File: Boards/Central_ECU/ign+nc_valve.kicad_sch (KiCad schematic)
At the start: 23 parts, among them J1 Safety interlock, U3 TPS16630PWPR, U4 LM339, U5 TPS16630PWPR

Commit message: Some more minor tweaks
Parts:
- removed C29: 100n, Capacitor_SMD:C_0805_2012Metric, symbol Device:C
- removed C32: 22u, Capacitor_SMD:C_0805_2012Metric, symbol Device:C
- removed J1: Safety interlock, symbol Connector:Screw_Terminal_01x02
- removed R16: 4K5, Resistor_SMD:R_0805_2012Metric, symbol Device:R
- removed R17: 47K, Resistor_SMD:R_0805_2012Metric, symbol Device:R
- removed U5: TPS16630PWPR, Package_SO:HTSSOP-20-1EP_4.4x6.5mm_P0.65mm_EP3.4x6.5mm_Mask2.96x2.96mm_ThermalVias, symbol Power_Management:TPS16630PWPR
- added C29: 50u, symbol Device:C_Polarized
- added D2: D_Zener, symbol Device:D_Zener
- added F1: 2A, symbol Device:Fuse
- added Q3: DMT12H060LFDF-7, Package_DFN_QFN:Diodes_UDFN2020-6_Type-F, symbol Simulation_SPICE:NMOS
- added R29: 3.3K, Resistor_SMD:R_0805_2012Metric, symbol Device:R
- added R30: 549, Resistor_SMD:R_0805_2012Metric, symbol Device:R
- added R7: 121R, symbol Device:R
- added R9: 1K40, symbol Device:R
- added U5: LM1084-ADJ, symbol Regulator_Linear:LM1084-ADJ
- C28: value ? -> 10u; footprint Capacitor_SMD:C_0805_2012Metric -> (none); now fitted; now in the parts list
- C30: value 100n -> 22u
- C31: value 10u -> 22u
- R11: value 10K -> 0R; footprint Resistor_SMD:R_0805_2012Metric -> (none)
- R12: value 47K -> 35K7
- R15: value 10k -> 0R; footprint Resistor_SMD:R_0805_2012Metric -> (none)
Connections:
- net GND: now also U4.12 (V-), C29.2, D2.2 (A), Q3.3 (S), Q3.8 (S), R29.1, R9.2; no longer R15.2
- net at C17.1, C20.1, R8.1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: now also R15.1
- net OX_SOLENOID_-: now reaches U4.11 (+)
- net OX_SOLENOID_-: now also D2.1 (K), Q3.1 (D), Q3.2 (D), Q3.5 (D), Q3.6 (D), Q3.7 (D)
- net OX_SOLENOID_+: now reaches C31.1
- net OX_SOLENOID_+: now also C30.1, F1.2
- net 4S_ARMED_V+: now reaches C28.1
- net 4S_ARMED_V+: now also U5.3 (VI)
- net at U4.9 (+): now also R11.1, R15.2, C29.1, R7.1, U5.2 (VO)
- net VDDIO: now reaches U4.3 (V+)
- net VDDIO: now also R10.1
- removed net +3V3: R10.1, R11.1
- removed net ARM_VALVE: C30.1, R15.1
- net PGOOD_VALVE: no longer names the net of R11.2
- net PGOOD_VALVE: now also F1.1
- new net: Q3.4 (G), R30.2
- new net: R7.2, R9.1, U5.1 (ADJ)
- new net OX_FIRE: R29.2, R30.1
- no-connect marks 6 -> 3
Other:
- note added: "12V Regulator"
- note added: "Efficiency with 4s lipo input: Worst case 12/16.8 = 71% Typical case 12/14.8 = 81% Max power loss (16w servo) = 6.6W"
- note added: "IMON gives (IOUT*27.9u)*R volts With R=35700 is 0.996V/A At 4A will give 4V which is safe for 5V tollerant pins"
- note added: "Output requires some ESR for stablilty, namely zero at 50kHz. Datasheet reccomends 10u tantalum or 50u electrolytic. Could also look at ceramic with series resistor as per https://www.ti.com/document-viewer/lit/html/SSZTBJ1"
- note added: "Oxidider Solenoid Control"
- note added: "Vout = 1.25(1+R2/R1)"
- note removed: "IMON gives (IOUT*27.9u)*R volts With R=47000 is 1.311V/A"
- note removed: "NC Solenoid Valve"
- moved on the sheet: C17, C18, C19, C20, C21, R10, R12, R13, R14, R8, U3, U4A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

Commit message: Added most connectors and hooking up
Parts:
- removed D2: D_Zener, symbol Device:D_Zener
- removed R11, R15: 0R, symbol Device:R
- added D2: D_Schottky, symbol Device:D_Schottky
- added R16, R17, R18: 0R, symbol Device:R
- R14: value 4K5 -> 6K2
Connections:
- net 4S_ARMED_V+: now also R16.1, R17.2; no longer C28.1, U5.3 (VI)
- net OX_SOLENOID_+: now also D2.1 (K)
- net OX_SOLENOID_-: now also D2.2 (A)
- net Pyro Low Side/Ign+: now also F1.1
- net VDDIO: now also U4.10 (-), U4.4 (-), U4.6 (-), U4.8 (-)
- net at C17.1, C20.1, R8.1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: now also U4.9 (+), R17.1, R18.2
- net OX_LOW_SENSE: now reaches U4.13
- net at C29.1, R7.1, U5.2 (VO): now also R18.1; no longer U4.9 (+)
- net EMATCH_2_CONT: now reaches U4.1
- net 12V_SENSE: now reaches U4.14
- net EMATCH_1_CONT: now reaches U4.2
- net ARM_IGN renamed ARM_HS
- net IMON_IGN renamed IMON_HS
- net PGOOD_IGN renamed PGOOD_HS
- new net: C28.1, R16.2, U5.3 (VI)
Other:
- note added: "Bypass to allow for externally regulated power to be passed directly through. This will be useful if a 24V solenoid is used."
- note added: "High Side Switch"
- note added: "NFET good for 4.3A and V_DS of 115V. Max pulse 20A for 10us, ~1W continuous power dissapation."
- note added: "Ox Solenoid Control"
- note added: "Set to 3A max current"
- note removed: "Oxidider Solenoid Control"
- note removed: "Set to 4A max current"
- moved on the sheet: C17, C18, C19, C20, C21, C28, C29, C30, C31, F1, Q3, R10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

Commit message: For review
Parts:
- removed Q3: DMT12H060LFDF-7, Package_DFN_QFN:Diodes_UDFN2020-6_Type-F, symbol Simulation_SPICE:NMOS
- added Q1: DMT12H060LFDF, Package_DFN_QFN:Diodes_UDFN2020-6_Type-F, symbol TS_Symbols:DMT12H060LFDF
- added TP29: 12V, TestPoint:TestPoint_Keystone_5005-5009_Compact, symbol Connector:TestPoint_Small
- added TP30: ARMED, TestPoint:TestPoint_Keystone_5005-5009_Compact, symbol Connector:TestPoint_Small
- C21: renamed from C28; footprint (none) -> Capacitor_SMD:C_0805_2012Metric
- C22: renamed from C29; footprint (none) -> Capacitor_SMD:CP_Elec_6.3x9.9; MPN (none) -> 865080645012
- D5: renamed from D2; footprint (none) -> Diode_SMD:D_SOD-882; MPN (none) -> CTS05S40,L3F
- F1: footprint (none) -> Fuse:Fuse_1206_3216Metric
- R20: renamed from R17; footprint (none) -> Resistor_SMD:R_0805_2012Metric
- R21: renamed from R16; footprint (none) -> Resistor_SMD:R_0805_2012Metric
- R22: renamed from R18; footprint (none) -> Resistor_SMD:R_0805_2012Metric
- R23: renamed from R7; footprint (none) -> Resistor_SMD:R_0805_2012Metric
- R24: renamed from R9; footprint (none) -> Resistor_SMD:R_0805_2012Metric
- U4: value LM339 -> LM339B; footprint (none) -> Package_SO:TSSOP-14_4.4x5mm_P0.65mm; MPN (none) -> LM339BIPWR
- U5: footprint (none) -> Package_TO_SOT_SMD:TO-263-3_TabPin2; MPN (none) -> LM1084ISX-ADJ/NOPB
- U6: renamed from U3; MPN (none) -> TPS16630PWPR
- renumbered C30 to C23, C31 to C24, C17 to C25, C20 to C26, C21 to C27, C19 to C28, C18 to C29, R30 to R25, R29 to R26, R8 to R27, R10 to R28, R12 to R29, R13 to R30, R14 to R31
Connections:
- net GND: now also Q1.4, Q1.8 (S)
- net OX_SOLENOID_-: now also Q1.1, Q1.2 (D), Q1.5 (D), Q1.6 (D), Q1.7 (D)
- net Pyro Low Side/Ign+: now also TP30.1
- net at C25.1, C26.1, R20.1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: now also TP29.1
- net at R25.2: now also Q1.3
- no-connect marks 3 -> 4
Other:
- company: (none) -> Hybrid Test Stand 2025
- title: (none) -> Interlocked Components

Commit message: Changed to 0603 passives and added NRST line
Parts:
- C21, C23, C24, C25, C26, C27, C28, C29: footprint Capacitor_SMD:C_0805_2012Metric -> Capacitor_SMD:C_0603_1608Metric
- R20, R21, R22, R23, R24, R25, R26, R27, R28, R29, R30, R31: footprint Resistor_SMD:R_0805_2012Metric -> Resistor_SMD:R_0603_1608Metric
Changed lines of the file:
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@@
 			)
 		)
-		(property "Footprint" "Capacitor_SMD:C_0805_2012Metric"
+		(property "Footprint" "Capacitor_SMD:C_0603_1608Metric"
 			(at 63.1952 181.61 0)
 			(effects
@@
 			)
 		)
-		(property "Footprint" "Resistor_SMD:R_0805_2012Metric"
+		(property "Footprint" "Resistor_SMD:R_0603_1608Metric"
 			(at 83.058 212.09 90)
 			(effects
@@
 			)
 		)
-		(property "Footprint" "Resistor_SMD:R_0805_2012Metric"
+		(property "Footprint" "Resistor_SMD:R_0603_1608Metric"
 			(at 44.45 65.278 90)
 			(effects
@@
 			)
 		)
-		(property "Footprint" "Resistor_SMD:R_0805_2012Metric"
+		(property "Footprint" "Resistor_SMD:R_0603_1608Metric"
 			(at 290.068 104.14 90)
 			(effects
@@
 			)
 		)
-		(property "Footprint" "Capacitor_SMD:C_0805_2012Metric"
+		(property "Footprint" "Capacitor_SMD:C_0603_1608Metric"
 			(at 74.6252 181.61 0)
 			(effects
@@
 			)
 		)
-		(property "Footprint" "Resistor_SMD:R_0805_2012Metric"
+		(property "Footprint" "Resistor_SMD:R_0603_1608Metric"
 			(at 71.882 80.01 90)
 			(effects
@@
 			)
 		)
-		(property "Footprint" "Resistor_SMD:R_0805_2012Metric"
+		(property "Footprint" "Resistor_SMD:R_0603_1608Metric"
 			(at 33.782 57.15 90)
 			(effects
@@
 			)
 		)
-		(property "Footprint" "Resistor_SMD:R_0805_2012Metric"
+		(property "Footprint" "Resistor_SMD:R_0603_1608Metric"
 			(at 85.852 67.31 90)
 			(effects
@@
 			)
 		)
-		(property "Footprint" "Resistor_SMD:R_0805_2012Metric"
+		(property "Footprint" "Resistor_SMD:R_0603_1608Metric"
 			(at 144.272 215.9 90)
 			(effects
@@
 			)
 		)
-		(property "Footprint" "Capacitor_SMD:C_0805_2012Metric"
+		(property "Footprint" "Capacitor_SMD:C_0603_1608Metric"
 			(at 152.0952 181.61 0)
 			(effects
@@
 			)
 		)
-		(property "Footprint" "Resistor_SMD:R_0805_2012Metric"
+		(property "Footprint" "Resistor_SMD:R_0603_1608Metric"
 			(at 115.57 160.528 90)
 			(effects
@@
 			)
 		)
-		(property "Footprint" "Capacitor_SMD:C_0805_2012Metric"
+		(property "Footprint" "Capacitor_SMD:C_0603_1608Metric"
 			(at 48.5648 200.66 0)
 			(effects
@@
 			)
 		)
-		(property "Footprint" "Capacitor_SMD:C_0805_2012Metric"
+		(property "Footprint" "Capacitor_SMD:C_0603_1608Metric"
 			(at 275.2852 71.12 0)
 			(effects
@@
 			)
 		)
-		(property "Footprint" "Resistor_SMD:R_0805_2012Metric"
+		(property "Footprint" "Resistor_SMD:R_0603_1608Metric"
 			(at 125.73 65.278 90)
 			(effects
@@
 			)
 		)
-		(property "Footprint" "Capacitor_SMD:C_0805_2012Metric"
+		(property "Footprint" "Capacitor_SMD:C_0603_1608Metric"
 			(at 70.1548 215.9 0)
 			(effects
@@
 			)
 		)
-		(property "Footprint" "Resistor_SMD:R_0805_2012Metric"
+		(property "Footprint" "Resistor_SMD:R_0603_1608Metric"
 			(at 304.8 97.028 90)
 			(effects
@@
 			)
 		)
-		(property "Footprint" "Resistor_SMD:R_0805_2012Metric"
+		(property "Footprint" "Resistor_SMD:R_0603_1608Metric"
 			(at 155.702 208.28 90)
 			(effects
@@
 			)
 		)
-		(property "Footprint" "Capacitor_SMD:C_0805_2012Metric"
+		(property "Footprint" "Capacitor_SMD:C_0603_1608Metric"
 			(at 263.8552 71.12 0)
 			(effects
@@
 			)
 		)
-		(property "Footprint" "Resistor_SMD:R_0805_2012Metric"
+		(property "Footprint" "Resistor_SMD:R_0603_1608Metric"
 			(at 155.702 191.77 90)
 			(effects
@@
 			)
 		)
-		(property "Footprint" "Capacitor_SMD:C_0805_2012Metric"
+		(property "Footprint" "Capacitor_SMD:C_0603_1608Metric"
 			(at 54.3052 71.12 0)
 			(effects

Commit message: More progress on layout
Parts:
- C26, C27: footprint Capacitor_SMD:C_0603_1608Metric -> Capacitor_SMD:C_1206_3216Metric
- R20, R21, R22: footprint Resistor_SMD:R_0603_1608Metric -> Resistor_SMD:R_1206_3216Metric
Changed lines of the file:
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@@
 			)
 		)
-		(property "Footprint" "Resistor_SMD:R_0603_1608Metric"
+		(property "Footprint" "Resistor_SMD:R_1206_3216Metric"
 			(at 44.45 65.278 90)
 			(effects
@@
 			)
 		)
-		(property "Footprint" "Capacitor_SMD:C_0603_1608Metric"
+		(property "Footprint" "Capacitor_SMD:C_1206_3216Metric"
 			(at 74.6252 181.61 0)
 			(effects
@@
 			)
 		)
-		(property "Footprint" "Resistor_SMD:R_0603_1608Metric"
+		(property "Footprint" "Resistor_SMD:R_1206_3216Metric"
 			(at 33.782 57.15 90)
 			(effects
@@
 			)
 		)
-		(property "Footprint" "Capacitor_SMD:C_0603_1608Metric"
+		(property "Footprint" "Capacitor_SMD:C_1206_3216Metric"
 			(at 152.0952 181.61 0)
 			(effects
@@
 			)
 		)
-		(property "Footprint" "Resistor_SMD:R_0603_1608Metric"
+		(property "Footprint" "Resistor_SMD:R_1206_3216Metric"
 			(at 125.73 65.278 90)
 			(effects

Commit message: Finished central ECU for review
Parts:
- TP29, TP30: footprint TestPoint:TestPoint_Keystone_5005-5009_Compact -> TestPoint:TestPoint_Pad_1.5x1.5mm
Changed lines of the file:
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@@
 	(title_block
 		(title "Interlocked Components")
-		(date "2025-04-02")
+		(date "2025-04-13")
 		(rev "A")
 		(company "Hybrid Test Stand 2025")
@@
 			)
 		)
-		(property "Footprint" "TestPoint:TestPoint_Keystone_5005-5009_Compact"
+		(property "Footprint" "TestPoint:TestPoint_Pad_1.5x1.5mm"
 			(at 182.88 173.99 0)
 			(effects
@@
 			)
 		)
-		(property "Footprint" "TestPoint:TestPoint_Keystone_5005-5009_Compact"
+		(property "Footprint" "TestPoint:TestPoint_Pad_1.5x1.5mm"
 			(at 143.51 101.6 0)
 			(effects

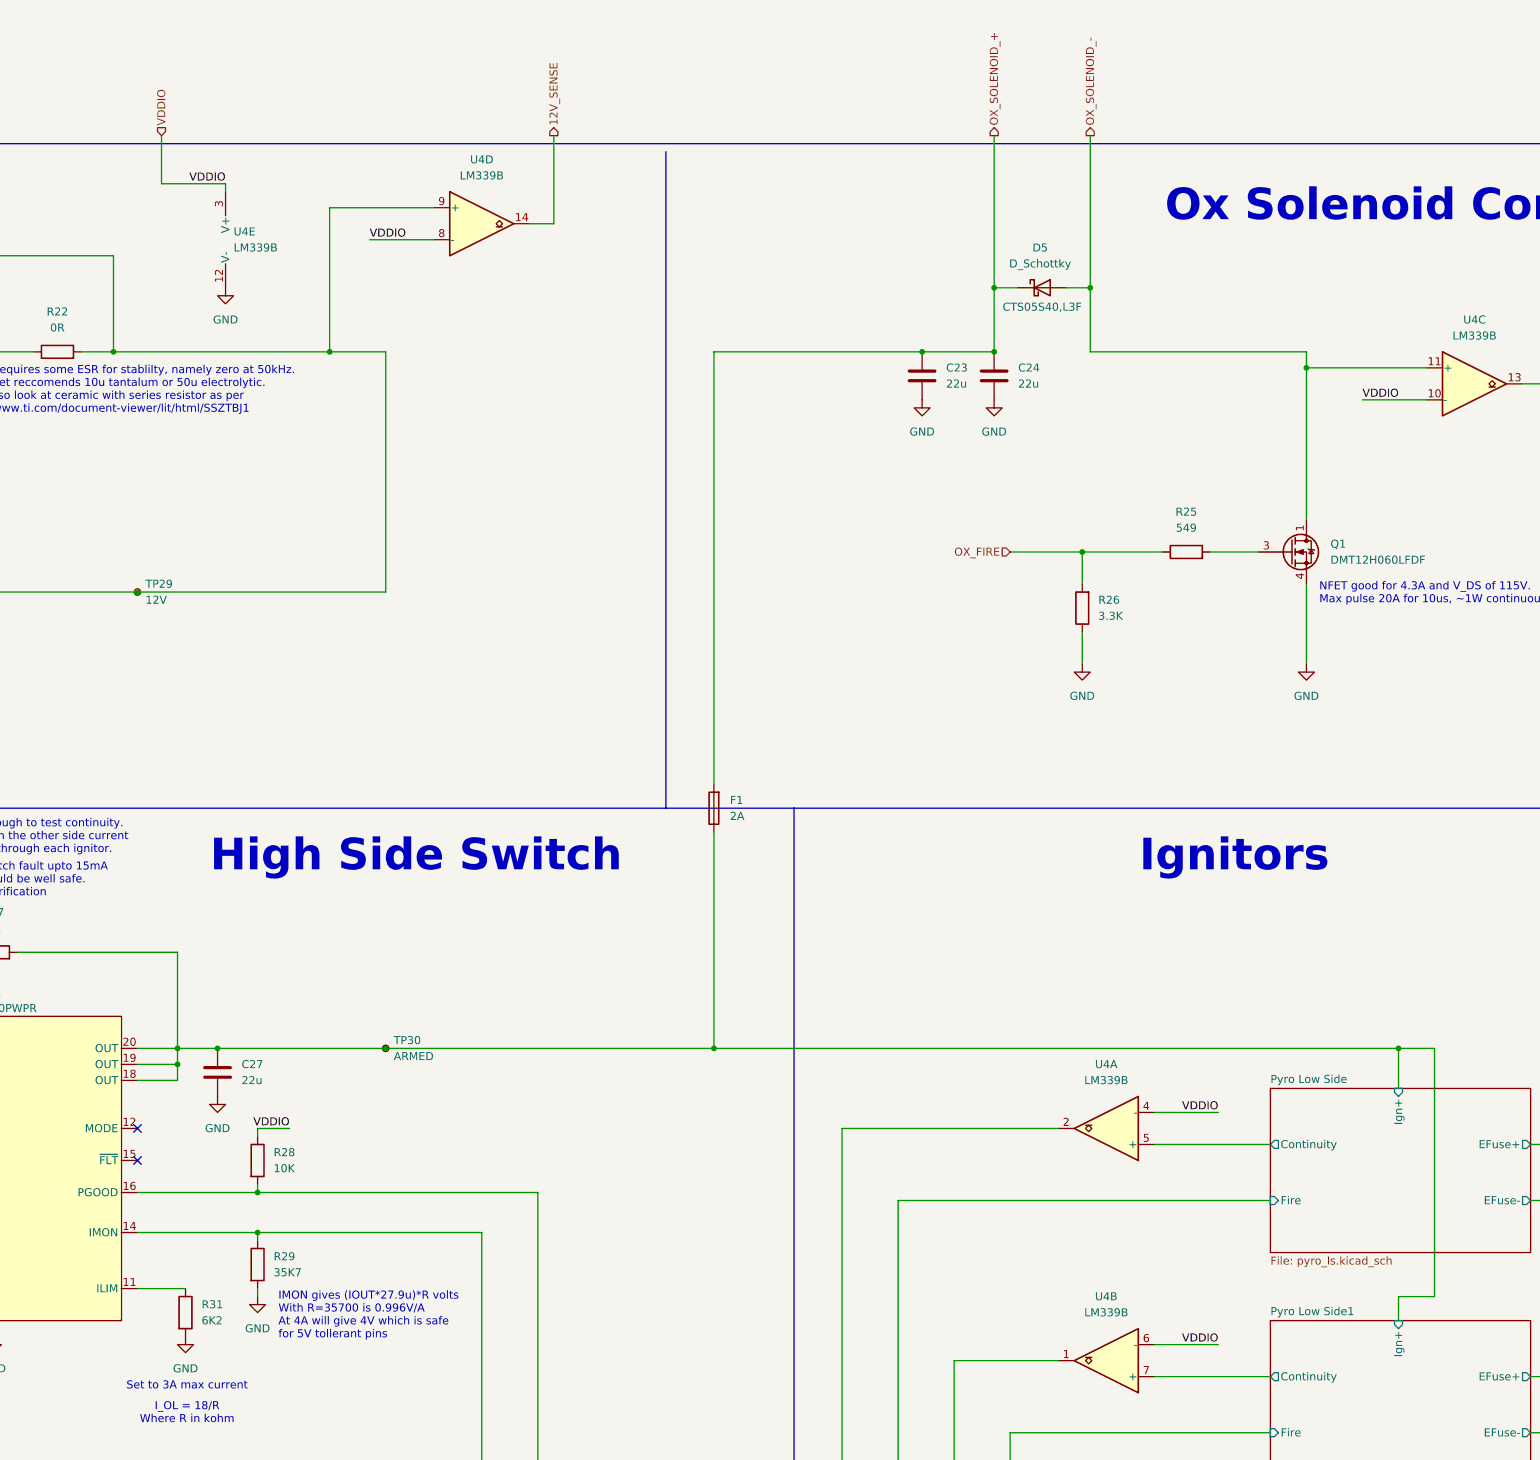
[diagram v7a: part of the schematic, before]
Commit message: Fixed voltage divider and comparator bias
Re feedback from Chris still need to fix regulator power dissipation. Happy with other points being non-issues at current.
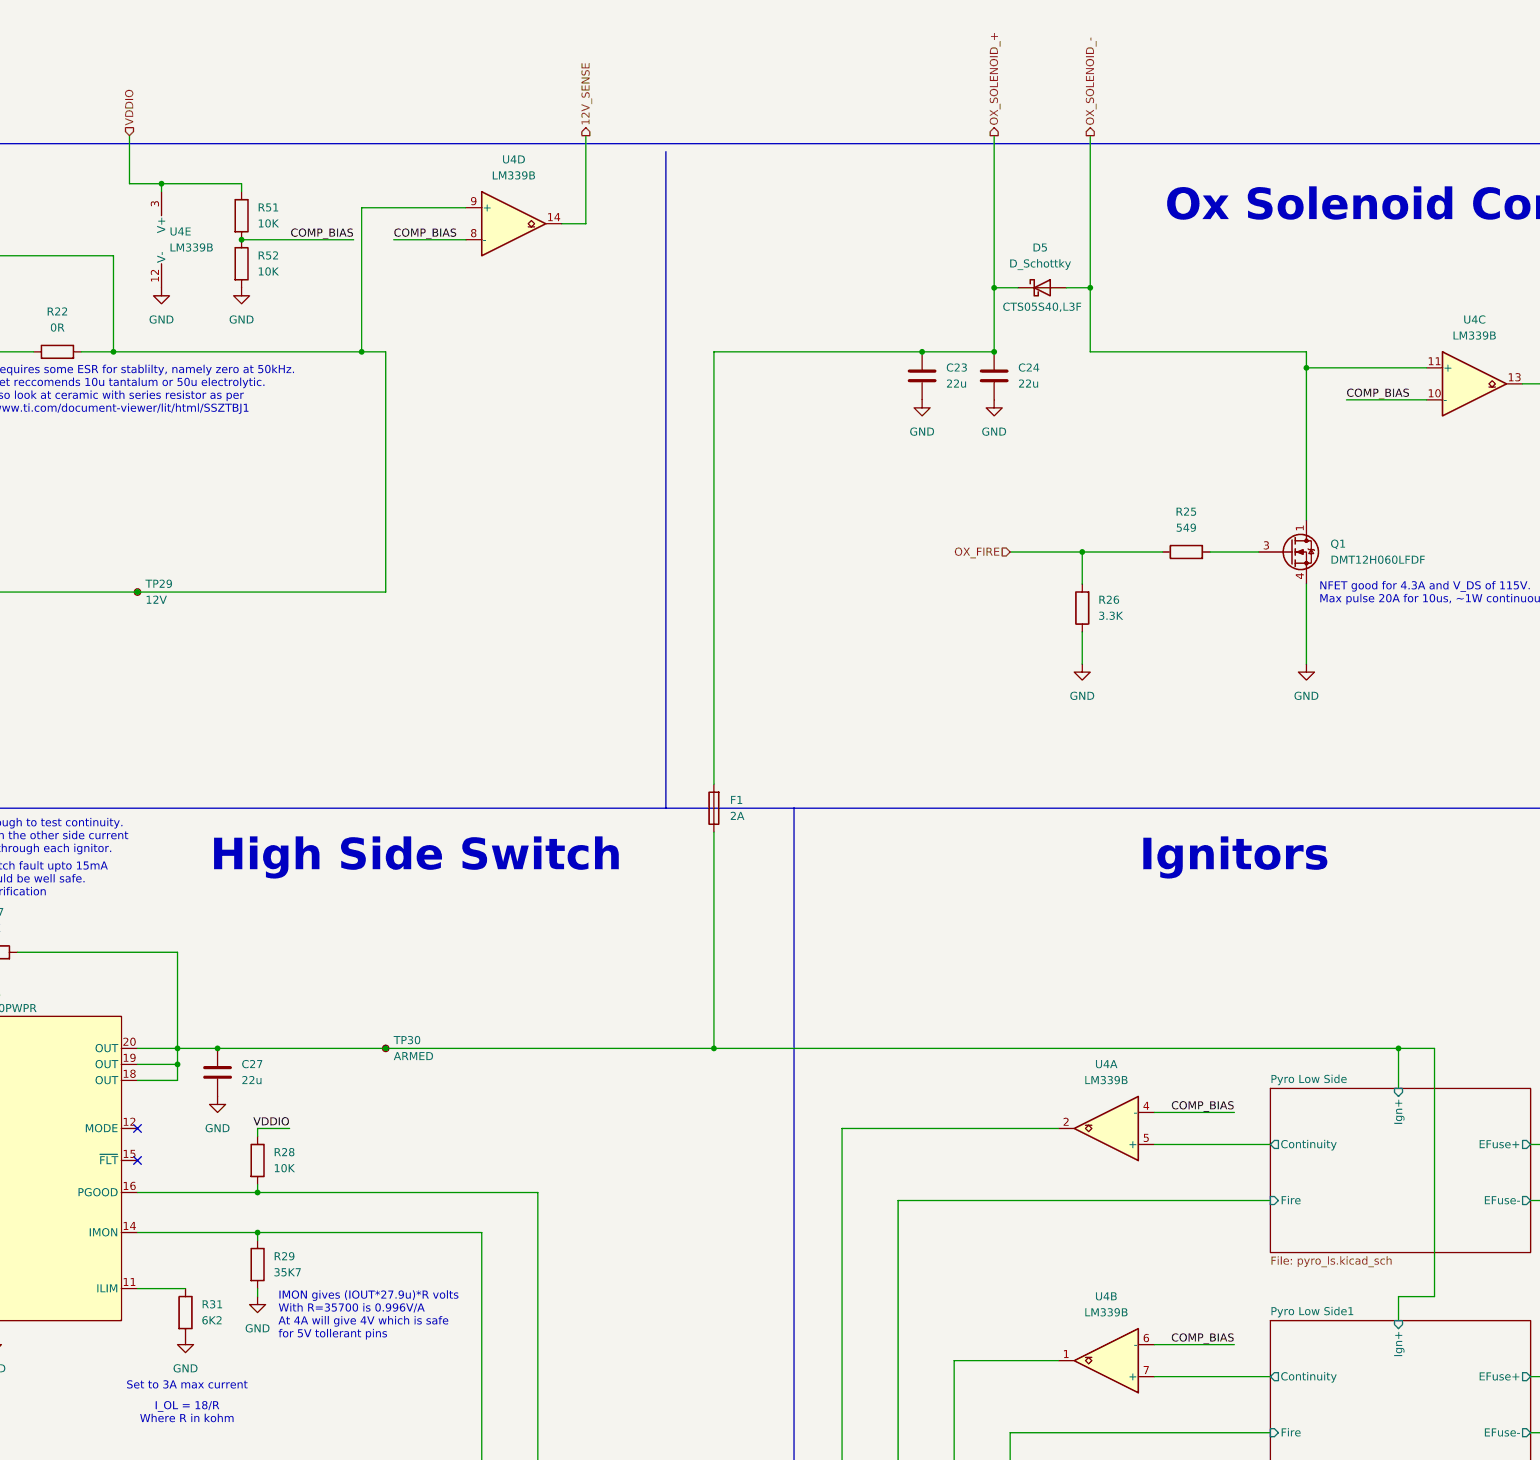
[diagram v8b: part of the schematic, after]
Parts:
- added R51, R52: 10K, Resistor_SMD:R_0603_1608Metric, symbol Device:R
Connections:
- net GND: now also R52.2
- net VDDIO: now also R51.1; no longer U4.10 (-), U4.4 (-), U4.6 (-), U4.8 (-)
- new net COMP_BIAS: R51.2, R52.1, U4.10 (-), U4.4 (-), U4.6 (-), U4.8 (-)
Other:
- moved on the sheet: U4D, U4E
